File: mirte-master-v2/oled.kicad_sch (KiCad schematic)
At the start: 1 part, among them J9 oled_conn

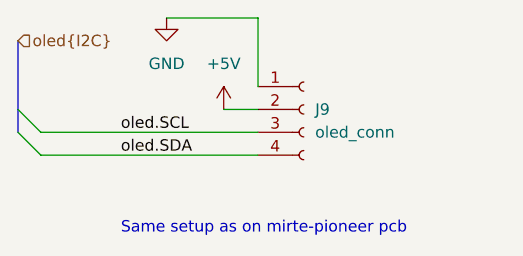
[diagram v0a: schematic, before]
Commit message: integrated the ina226 in the pcb layout
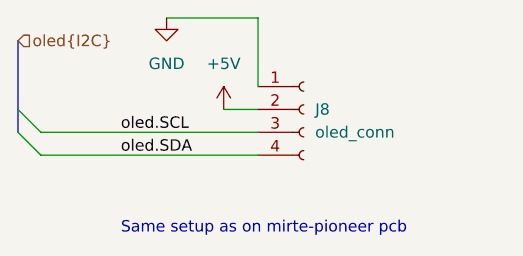
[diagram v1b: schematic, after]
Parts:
- renumbered J9 to J8
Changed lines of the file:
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@@
 		(dnp no)
 		(fields_autoplaced yes)
-		(property "Reference" "J9"
+		(property "Reference" "J8"
 			(at 144.78 60.96 0)
 			(effects
@@
 			(project "mirte-master"
 				(path "/19794465-0368-488c-958e-83b02754ebd6/92d73fdd-79ea-46c8-8ce1-51296b6a6824"
-					(reference "J9")
+					(reference "J8")
 					(unit 1)
 				)
